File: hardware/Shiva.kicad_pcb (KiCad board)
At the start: 2 copper layers, 99.8 x 99.8 mm, 77 parts, among them J1 JACK_FEMALE_STEREO, J2 JACK_FEMALE_STEREO, J3 JACK_FEMALE_STEREO, J4 JACK_FEMALE_STEREO, J5 JACK_FEMALE_STEREO, J6 JACK_FEMALE_STEREO, J7 JACK_FEMALE_STEREO, J8 JACK_FEMALE_STEREO, P1 DIN_5, U1 LTC6242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

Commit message: Route channel 1
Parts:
- moved D7 8.80 mm to (109.5, 134.2)
- moved R8 4.34 mm to (102.3, 134.2), turned to 90 degrees
- moved JP4 4.29 mm to (98.9, 137.4)
- moved R12 4.15 mm to (103.6, 139.3), turned to 180 degrees
- moved D8 3.31 mm to (107.3, 134.2), turned to 90 degrees
- moved R4 1.97 mm to (104.9, 134.2), turned to 90 degrees
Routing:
- net /CHANNEL_01: track 25.2 -> 94.5 mm
- net Net-(D7-Pad2): track 64.0 -> 90.5 mm, vias 2 -> 0
- net Net-(R12-Pad2): track 58.4 -> 81.4 mm, vias 2 -> 0
- net VCC: track 416.8 -> 425.1 mm
- net Net-(J4-PadTS): track 3.83 -> 0.00 mm
- net /DETECT_01: track 5.47 -> 2.12 mm
- net GND: track 251.1 -> 248.8 mm

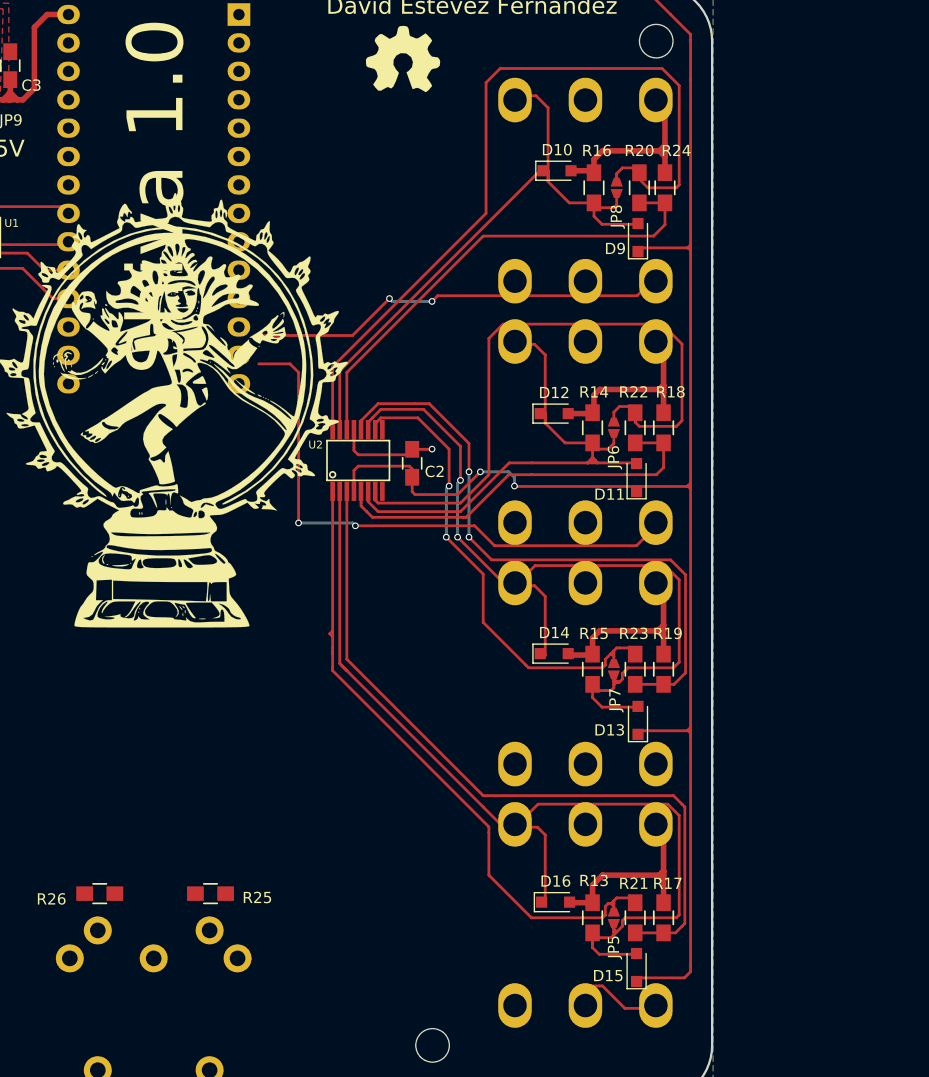
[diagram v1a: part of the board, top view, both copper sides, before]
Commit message: Route channel 5, swap channels to simplify op-amp routing
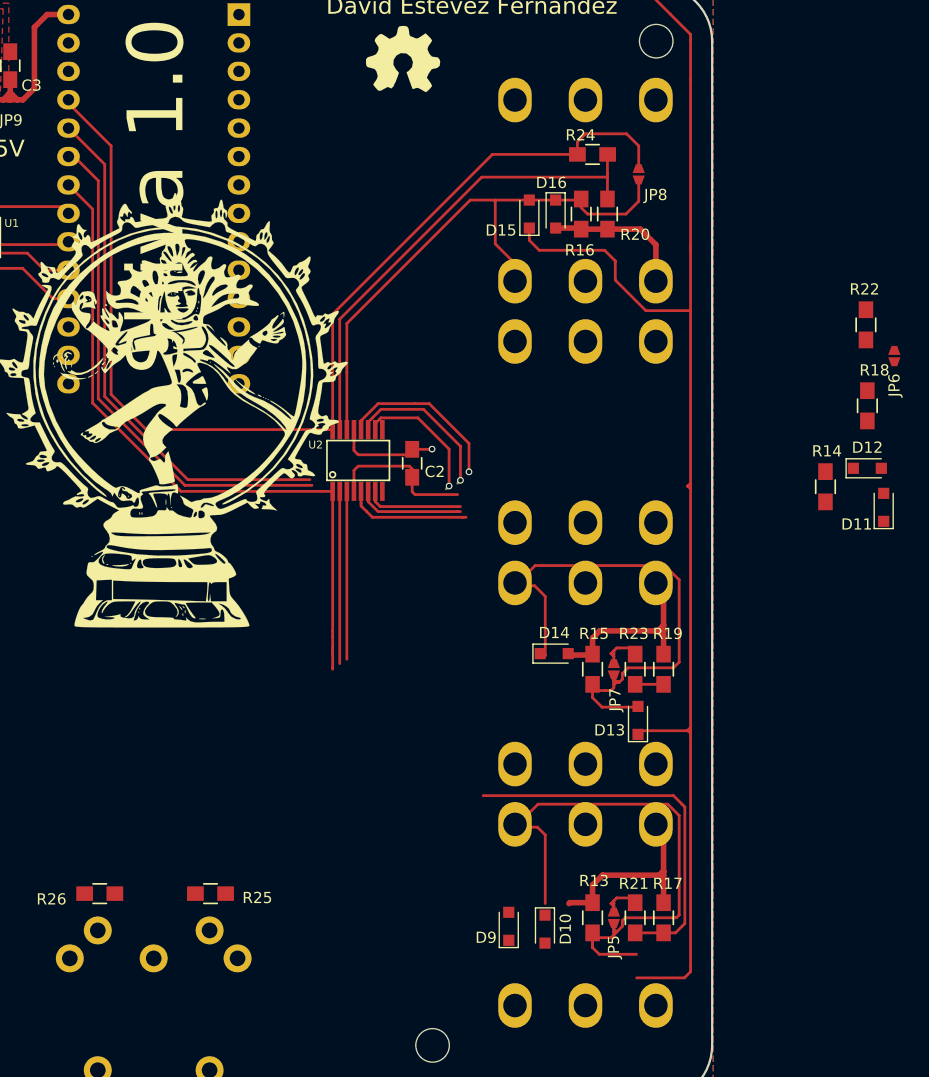
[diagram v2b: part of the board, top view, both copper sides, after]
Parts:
- moved D15 68.1 mm to (177.9, 73.2)
- moved D10 67.8 mm to (179.3, 137.2), turned to 270 degrees
- moved D9 62.7 mm to (176.0, 136.9)
- moved D16 61.5 mm to (180.2, 73.2), turned to 270 degrees
- moved D12 28.4 mm to (208.1, 95.9)
- moved JP6 25.9 mm to (210.5, 85.9)
- moved R22 22.6 mm to (208.0, 83.1)
- moved D11 22.3 mm to (209.6, 99.4)
- moved R14 21.5 mm to (204.3, 97.6)
- moved R18 18.3 mm to (208.1, 90.4)
- moved R20 5.65 mm to (184.8, 73.2), turned to 270 degrees
- moved R24 5.15 mm to (183.5, 67.9), turned to 0 degrees
- moved R16 2.61 mm to (182.5, 73.2), turned to 270 degrees
- moved JP8 2.31 mm to (187.6, 69.7)
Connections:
- J5 pad SS: /DETECT_08 -> /DETECT_05
- J5 pad T: Net-(D10-Pad1) -> Net-(D15-Pad2)
- J8 pad SS: /DETECT_05 -> /DETECT_08
- J8 pad T: Net-(D15-Pad2) -> Net-(D10-Pad1)
- U2 pad 10: /CHANNEL_07 -> /CHANNEL_06
- U2 pad 11: Net-(R19-Pad1) -> Net-(R18-Pad1)
- U2 pad 12: Net-(D13-Pad2) -> Net-(D11-Pad2)
- U2 pad 5: Net-(D11-Pad2) -> Net-(D13-Pad2)
- U2 pad 6: Net-(R18-Pad1) -> Net-(R19-Pad1)
- U2 pad 7: /CHANNEL_06 -> /CHANNEL_07
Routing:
- net GND: track 248.8 -> 138.9 mm, vias 7 -> 3
- net Net-(D10-Pad1): track 140.1 -> 54.8 mm
- net Net-(D11-Pad2): track 73.6 -> 15.4 mm, vias 0 -> 1
- net Net-(D13-Pad2): track 67.8 -> 27.0 mm, vias 2 -> 0
- net Net-(R20-Pad1): track 9.76 -> 43.4 mm
- net /CHANNEL_06: track 28.7 -> 59.2 mm, vias 0 -> 1
- net Net-(R17-Pad1): track 20.1 -> 49.3 mm
- net /CHANNEL_05: track 72.1 -> 96.8 mm
- net Net-(J7-PadTS): track 29.0 -> 5.09 mm, vias 2 -> 0
- net Net-(J6-PadTS): track 17.8 -> 0.00 mm
- net /DETECT_06: track 18.8 -> 1.76 mm
- net /CHANNEL_07: track 44.5 -> 60.0 mm, vias 2 -> 0
- net Net-(J8-PadTS): track 27.4 -> 13.1 mm
- net VCC: track 425.1 -> 416.3 mm, vias 4 -> 2
- net Net-(R19-Pad1): track 4.97 -> 12.4 mm
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
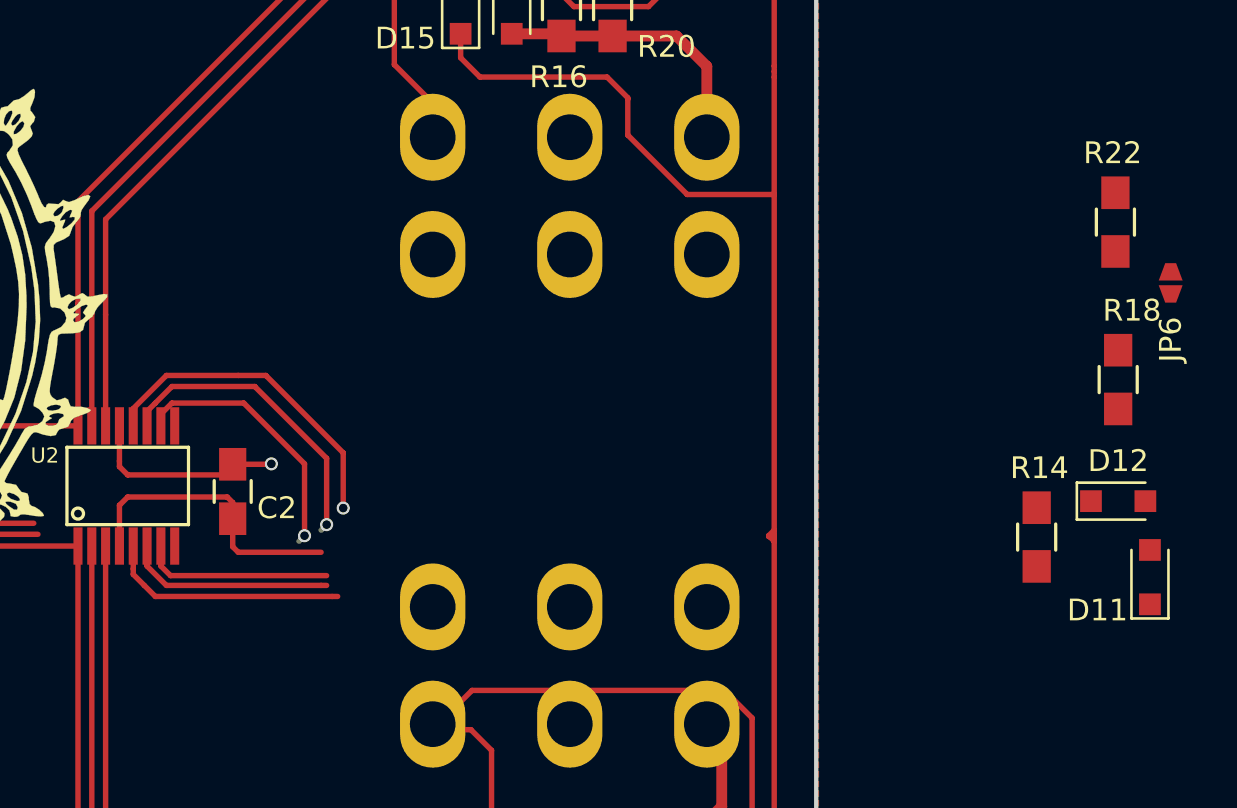
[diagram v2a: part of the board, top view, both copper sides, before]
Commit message: Route channel 6
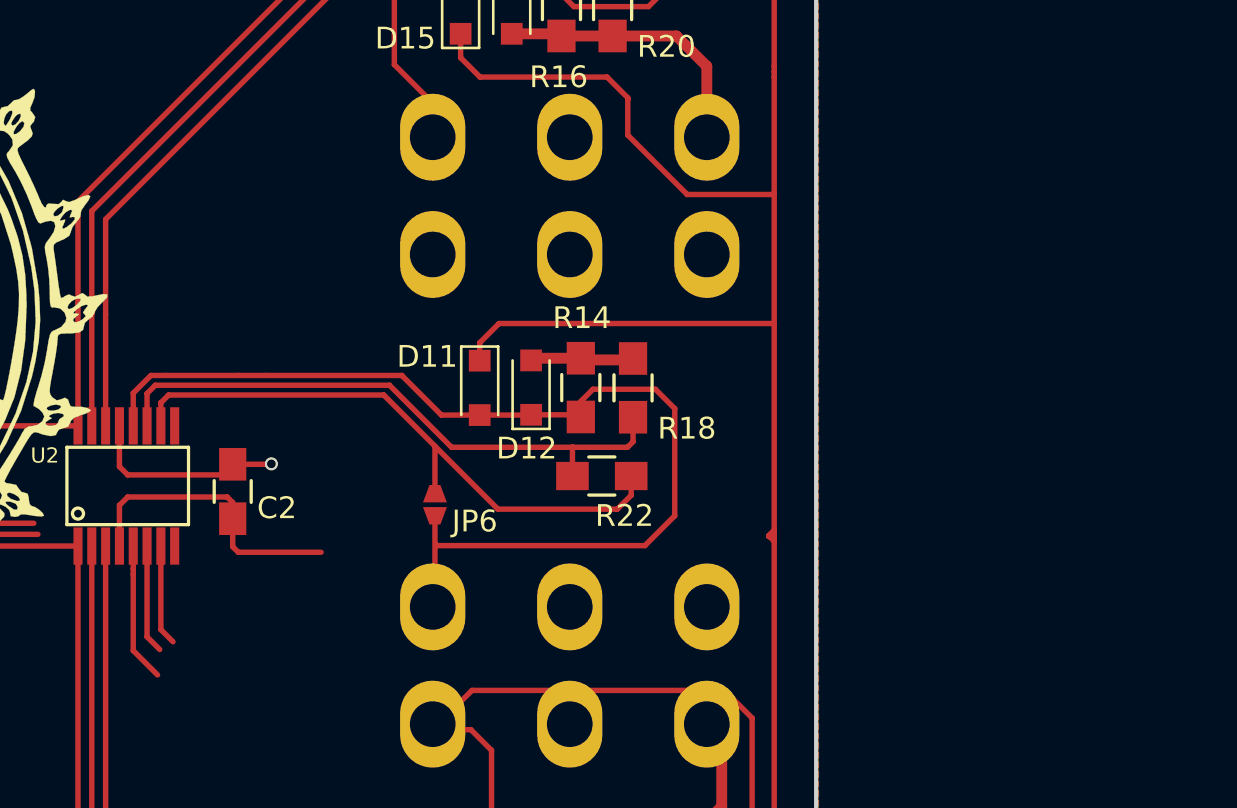
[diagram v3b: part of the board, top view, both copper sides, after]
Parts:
- moved JP6 35.3 mm to (176.7, 96.1)
- moved D11 32.0 mm to (178.7, 90.7), turned to 270 degrees
- moved D12 27.5 mm to (181.1, 90.7), turned to 90 degrees
- moved R22 26.3 mm to (184.4, 94.8), turned to 180 degrees
- moved R18 22.3 mm to (185.8, 90.7)
- moved R14 22.1 mm to (183.4, 90.7)
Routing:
- net Net-(D11-Pad2): track 15.4 -> 51.0 mm, vias 1 -> 0
- net /CHANNEL_06: track 59.2 -> 75.9 mm, vias 1 -> 0
- net VCC: track 416.3 -> 431.1 mm
- net Net-(R18-Pad1): track 14.5 -> 28.7 mm, vias 1 -> 0
- net GND: track 138.9 -> 143.8 mm
- net Net-(D13-Pad2): track 27.0 -> 22.3 mm
- net /CHANNEL_07: track 60.0 -> 55.9 mm
- net Net-(R19-Pad1): track 12.4 -> 8.62 mm

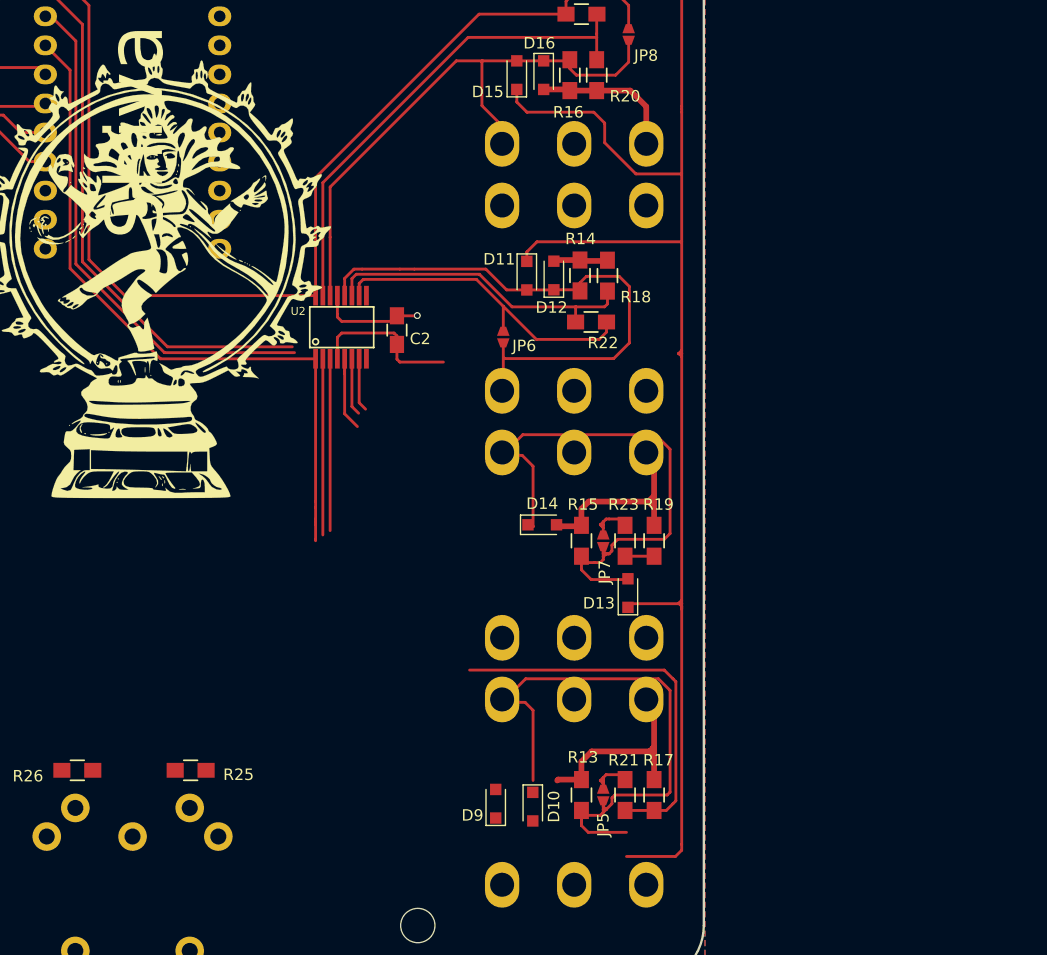
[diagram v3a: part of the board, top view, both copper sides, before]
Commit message: Route channel 7
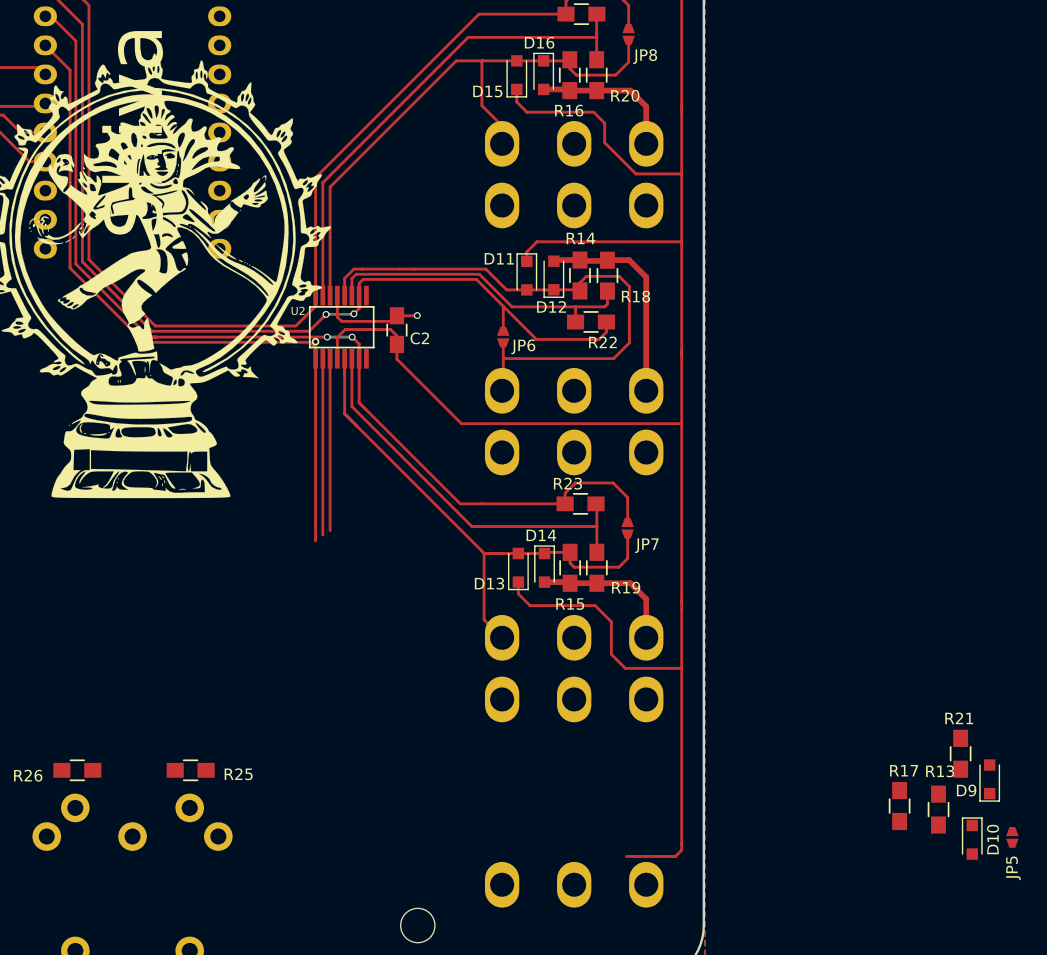
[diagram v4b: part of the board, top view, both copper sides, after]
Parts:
- moved D9 43.2 mm to (219.2, 134.8)
- moved D10 38.5 mm to (217.7, 140.1)
- moved JP5 36.0 mm to (221.2, 139.9)
- moved R13 31.2 mm to (214.7, 137.4)
- moved R21 29.6 mm to (216.7, 132.5)
- moved R17 21.5 mm to (211.3, 137.1)
- moved D13 9.83 mm to (178.0, 116.3)
- moved R19 5.53 mm to (184.9, 116.3), turned to 270 degrees
- moved R23 5.05 mm to (183.4, 110.7), turned to 0 degrees
- moved D14 3.76 mm to (180.3, 116.3), turned to 270 degrees
- moved R15 2.56 mm to (182.5, 116.3), turned to 270 degrees
- moved JP7 2.40 mm to (187.6, 112.8)
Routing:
- net Net-(D10-Pad1): track 54.8 -> 15.3 mm
- net VCC: track 431.1 -> 467.1 mm
- net Net-(R17-Pad1): track 49.3 -> 15.7 mm
- net /CHANNEL_07: track 55.9 -> 89.5 mm, vias 0 -> 2
- net /DETECT_07: track 34.3 -> 2.12 mm
- net Net-(D13-Pad2): track 22.3 -> 49.6 mm
- net Net-(R19-Pad1): track 8.62 -> 35.3 mm
- net Net-(J8-PadTS): track 13.1 -> 0.00 mm
- net /CHANNEL_06: track 75.9 -> 83.2 mm, vias 0 -> 2
- net /DETECT_08: track 5.47 -> 1.15 mm
- net Net-(J7-PadTS): track 5.09 -> 0.78 mm
- net /CHANNEL_08: track 65.5 -> 61.9 mm
- net GND: track 143.8 -> 140.7 mm
- net /CHANNEL_05: track 96.8 -> 99.6 mm

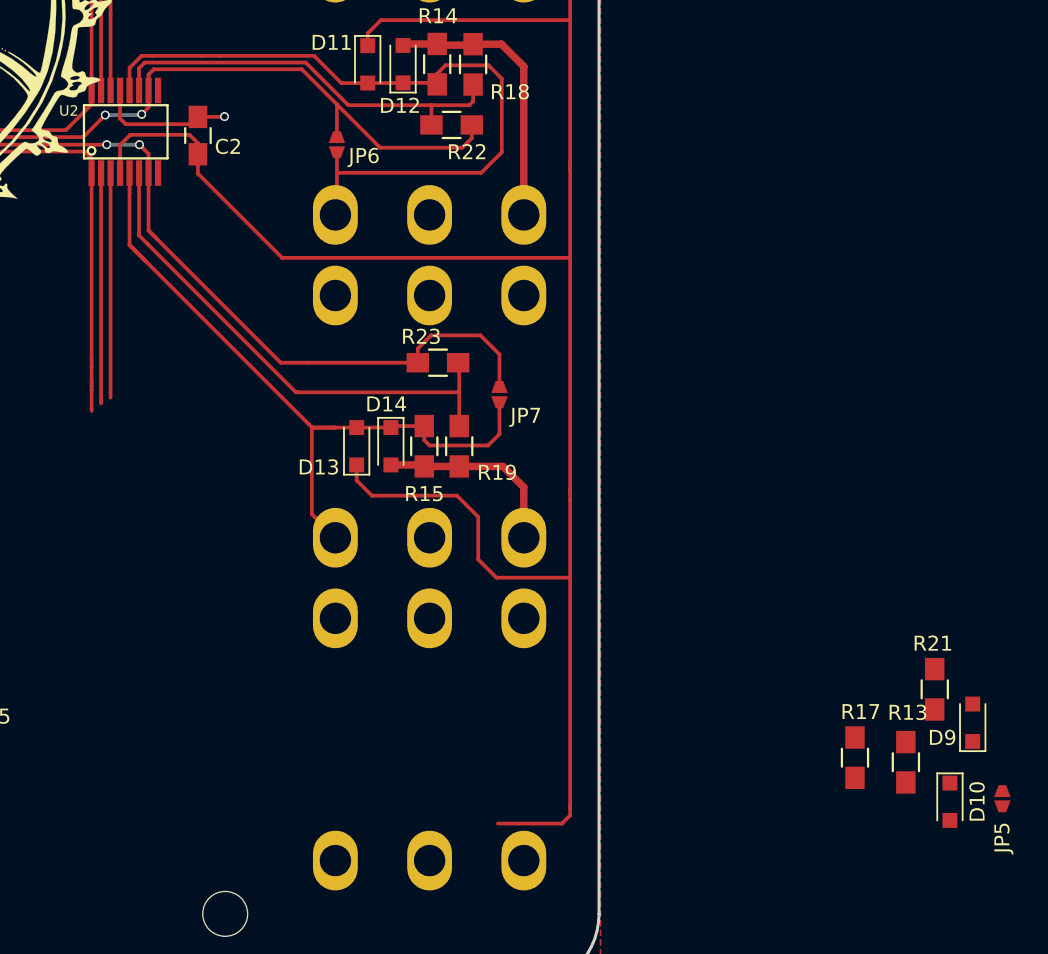
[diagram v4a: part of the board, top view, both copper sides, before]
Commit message: Route channel 8
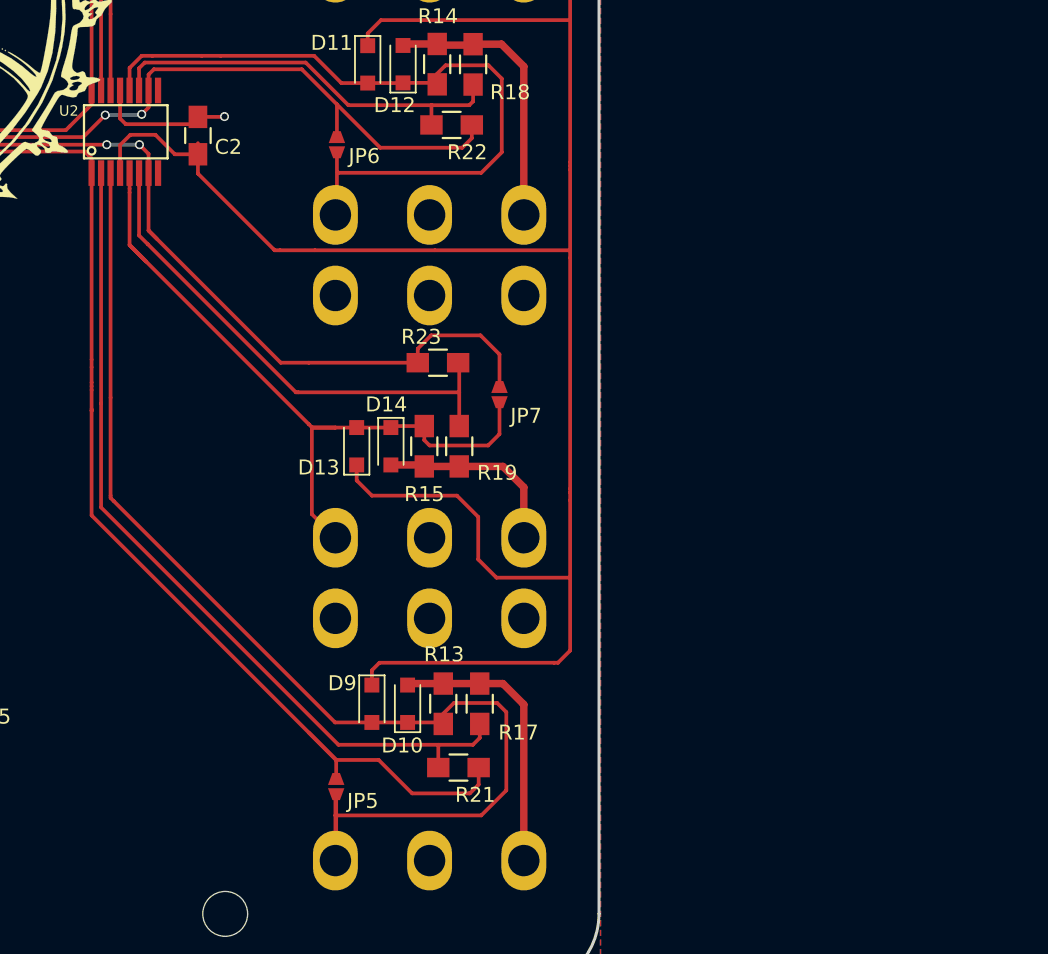
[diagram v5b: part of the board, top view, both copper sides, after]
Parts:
- moved JP5 44.6 mm to (176.6, 139.0)
- moved D9 40.2 mm to (179.0, 133.5), turned to 270 degrees
- moved D10 36.9 mm to (181.4, 133.5), turned to 90 degrees
- moved R21 32.3 mm to (184.8, 137.8), turned to 180 degrees
- moved R13 31.2 mm to (183.8, 133.5)
- moved R17 25.4 mm to (186.2, 133.5)
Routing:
- net Net-(D10-Pad1): track 15.3 -> 80.7 mm
- net /CHANNEL_08: track 61.9 -> 107.7 mm
- net Net-(R17-Pad1): track 15.7 -> 57.2 mm
- net GND: track 140.7 -> 159.6 mm
- net VCC: track 467.1 -> 465.9 mm
